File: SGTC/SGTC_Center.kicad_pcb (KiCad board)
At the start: 2 copper layers, 152.4 x 63.5 mm, 17 parts, among them J1 Left, J2 Right, U1 ADS8691IPWR, U2 TMUX131RMG, U3 SN74HCS72QDRQ1, U4 74AHC1G00, U5 AD8421

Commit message: added schematic to new SGTC
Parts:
- moved U4 3.67 mm to (143.6, 109.8)
- moved J1 3.67 mm to (120.1, 98.2)
- moved R2 3.67 mm to (117.9, 100.7)
- moved C4 3.67 mm to (125.9, 106.9)
- moved C5 3.67 mm to (122.7, 100.7)
- moved C6 3.67 mm to (117.9, 108.2)
- moved J2 3.67 mm to (140.4, 111.0)
- moved U1 3.67 mm to (120.4, 104.5)
- moved U5 3.67 mm to (130.1, 105.3)
- moved U2 3.67 mm to (133.4, 102.1)
- moved C1 3.67 mm to (127.2, 102.8)
- moved C2 3.67 mm to (125.2, 102.8)
- moved C3 3.67 mm to (125.9, 105.3)
- moved C7 3.67 mm to (132.6, 107.0)
- moved C8 3.67 mm to (134.6, 107.0)
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
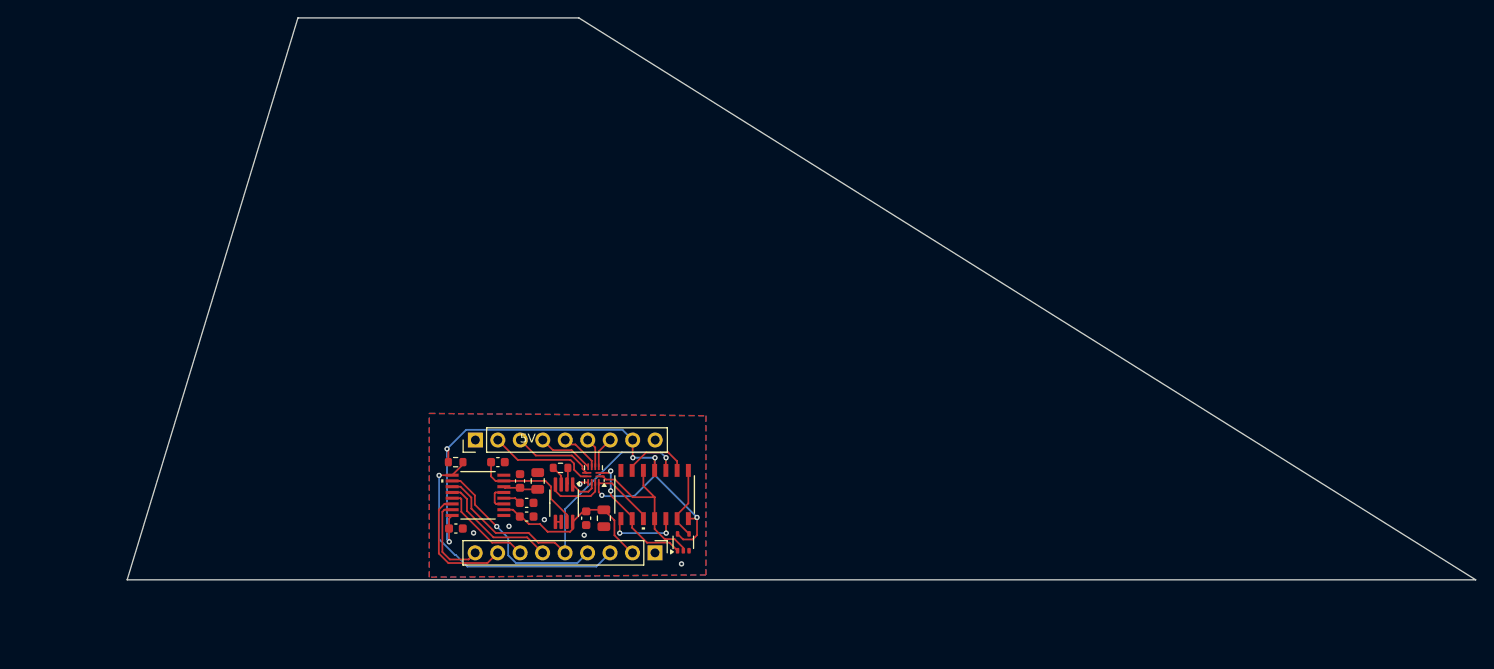
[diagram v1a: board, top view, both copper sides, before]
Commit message: fin center draft
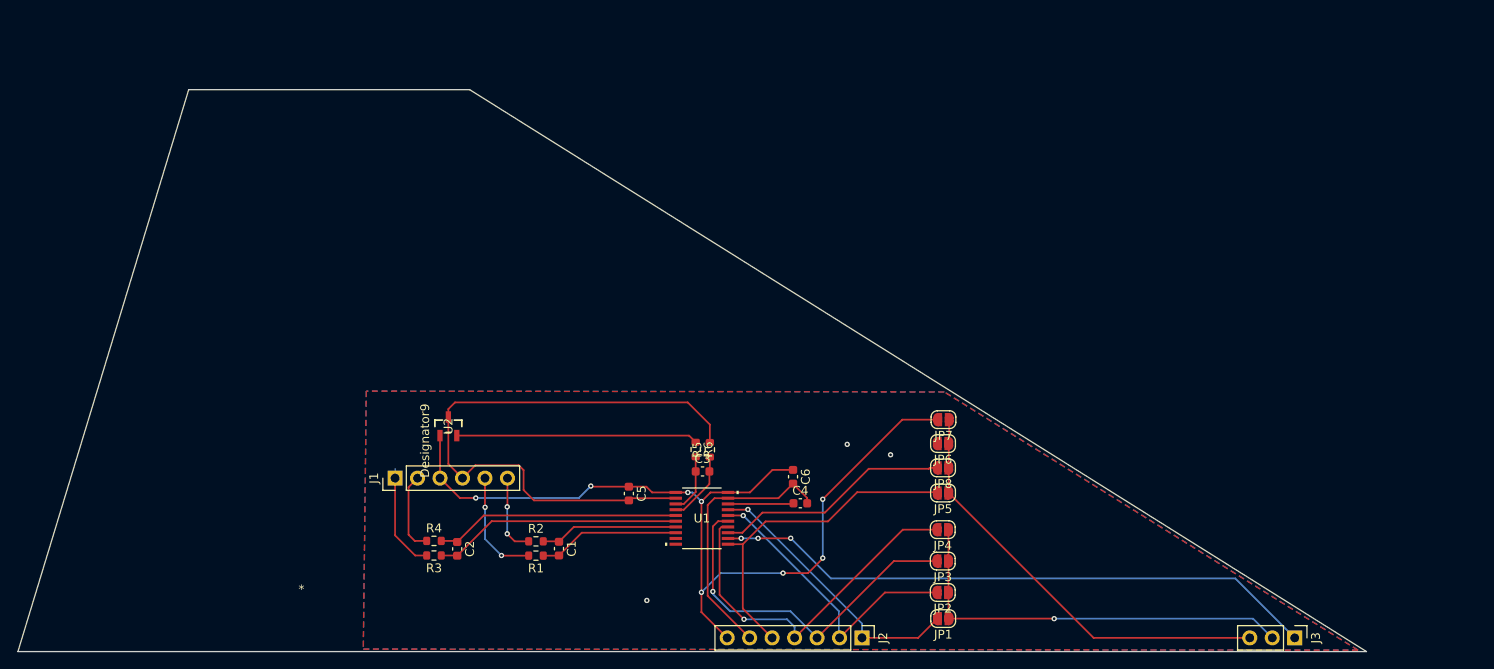
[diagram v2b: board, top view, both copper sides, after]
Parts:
- removed C7: 0.1 uF, Capacitor_SMD:C_0603_1608Metric
- removed C8: 10 uF, Capacitor_SMD:C_0805_2012Metric
- removed U3: SN74HCS72QDRQ1, strain-gauge:SOIC_QDRQ1_TEX
- removed U4: 74AHC1G00, Package_TO_SOT_SMD:SOT-353_SC-70-5
- removed U5: AD8421, Package_SO:MSOP-8_3x3mm_P0.65mm
- added J3: Conn_01x03_Pin, Connector_PinHeader_2.54mm:PinHeader_1x03_P2.54mm_Vertical, F.Cu at (212.7, 120.6)
- added JP1: SolderJumper_2_Open, Jumper:SolderJumper-2_P1.3mm_Open_RoundedPad1.0x1.5mm, F.Cu at (173.0, 118.4)
- added JP2: SolderJumper_2_Open, Jumper:SolderJumper-2_P1.3mm_Open_RoundedPad1.0x1.5mm, F.Cu at (172.9, 115.4)
- added JP3: SolderJumper_2_Open, Jumper:SolderJumper-2_P1.3mm_Open_RoundedPad1.0x1.5mm, F.Cu at (172.9, 111.9)
- added JP4: SolderJumper_2_Open, Jumper:SolderJumper-2_P1.3mm_Open_RoundedPad1.0x1.5mm, F.Cu at (172.9, 108.3)
- added JP5: SolderJumper_2_Open, Jumper:SolderJumper-2_P1.3mm_Open_RoundedPad1.0x1.5mm, F.Cu at (172.9, 104.2)
- added JP6: SolderJumper_2_Open, Jumper:SolderJumper-2_P1.3mm_Open_RoundedPad1.0x1.5mm, F.Cu at (172.9, 98.6)
- added JP7: SolderJumper_2_Open, Jumper:SolderJumper-2_P1.3mm_Open_RoundedPad1.0x1.5mm, F.Cu at (173.0, 95.9)
- added JP8: SolderJumper_2_Open, Jumper:SolderJumper-2_P1.3mm_Open_RoundedPad1.0x1.5mm, F.Cu at (172.9, 101.3)
- added R3: 10 k, Resistor_SMD:R_0603_1608Metric, F.Cu at (115.4, 111.2)
- added R4: 10 k, Resistor_SMD:R_0603_1608Metric, F.Cu at (115.4, 109.6)
- added R5: 10 k, Resistor_SMD:R_0603_1608Metric, F.Cu at (146.6, 99.3)
- added R6: 10 k, Resistor_SMD:R_0603_1608Metric, F.Cu at (145.0, 99.3)
- C1: value 10 uF -> 10 nF; footprint Capacitor_SMD:C_0805_2012Metric -> Capacitor_SMD:C_0603_1608Metric
- C2: value 1 uF -> 10 nF
- C3: value 4.7 uF -> 10 nF
- C4: value 1 uF -> 220 nF
- J1: value Left -> Conn_01x06_Pin; footprint Connector_PinHeader_2.54mm:PinHeader_1x09_P2.54mm_Vertical -> Connector_PinHeader_2.54mm:PinHeader_1x06_P2.54mm_Vertical
- J2: value Right -> Conn_01x07_Pin; footprint Connector_PinHeader_2.54mm:PinHeader_1x09_P2.54mm_Vertical -> Connector_PinHeader_2.54mm:PinHeader_1x07_P2.54mm_Vertical
- R1: value 100 -> 10 k
- R2: value 100k -> 10 k
- U1: value ADS8691IPWR -> ADS131M03QPWRQ1; footprint strain-gauge:PW16_TEX -> FinLib:ADS131M03
- U2: value TMUX131RMG -> TMP235A4DBZR; footprint Package_DFN_QFN:Texas_RMG0012A_WQFN-12_1.8x1.8mm_P0.4mm -> FinLib:TMP235A4DBZR
- moved C6 38.5 mm to (156.0, 102.3), turned to -90 degrees
- moved C4 31.0 mm to (156.8, 105.3)
- moved U1 25.4 mm to (145.7, 107.0), turned to 0 degrees
- moved J2 25.3 mm to (163.8, 120.6)
- moved C3 20.2 mm to (145.8, 101.8)
- moved U2 17.3 mm to (117.0, 96.7), turned to 90 degrees
- moved C5 15.2 mm to (137.4, 104.2), turned to -90 degrees
- moved R2 12.7 mm to (127.0, 109.7), turned to 0 degrees
- moved C2 10.5 mm to (118.0, 110.5)
- moved R1 10.3 mm to (127.0, 111.3)
- moved J1 10.0 mm to (111.0, 102.5)
- moved C1 8.02 mm to (129.6, 110.5)
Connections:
- net /ADC/~{CS} renamed ~{SYNC}/~{RST}
- C1 pad 1: GND -> Net-(U1-AIN2P)
- C1 pad 2: Net-(U1-REFCAP) -> Net-(U1-AIN2N)
- C2 pad 1: GND -> Net-(U1-AIN1N)
- C2 pad 2: Net-(U1-REFCAP) -> Net-(U1-AIN1P)
- C3 pad 1: Net-(U1-REFIO) -> Net-(U1-AIN0P)
- C3 pad 2: GND -> Net-(U1-AIN0N)
- C4 pad 1: +5V -> Net-(U1-CAP)
- C4 pad 2: GND -> TMP_IN_N
- C5 pad 1: /ADC/A_IN -> +3.3V
- C5 pad 2: GND -> TMP_IN_N
- C6 pad 1: GND -> +3.3V
- C6 pad 2: +3.3V -> TMP_IN_N
- J1 pad 1: GND -> GAUGE1_IN_N
- J1 pad 2: /Multiplexer/A_IN_N1 -> GAUGE1_IN_P
- J1 pad 3: /Multiplexer/A_IN_P1 -> +3.3V
- J1 pad 4: /Multiplexer/A_IN_N3 -> TMP_IN_N
- J1 pad 5: /Multiplexer/A_IN_P3 -> GAUGE2_IN_N
- J1 pad 6: /Multiplexer/A_IN_N2 -> GAUGE2_IN_P
- J2 pad 1: GND -> ADCCLK
- J2 pad 2: +5V -> DIN
- J2 pad 3: /ADC/~{RST} -> DOUT
- J2 pad 4: /ADC/SDI -> SPICLK
- J2 pad 6: /ADC/SCLK -> TMP_IN_N
- J2 pad 7: /ADC/SDO-0 -> +3.3V
- R1 pad 1: Net-(R1-Pad1) -> Net-(U1-AIN2N)
- R1 pad 2: Net-(R1-Pad2) -> GAUGE2_IN_N
- R2 pad 1: /ADC/~{RST} -> GAUGE2_IN_P
- R2 pad 2: +3.3V -> Net-(U1-AIN2P)
- U1 pad 1: GND -> +3.3V
- U1 pad 10: /ADC/SDI -> unconnected-(U1-NC-Pad10)
- U1 pad 12: /ADC/SCLK -> ~{CS}
- U1 pad 13: /ADC/SDO-0 -> ~{DRDY}
- U1 pad 14: /ADC/SDO-1 -> SPICLK
- U1 pad 15: /ADC/RVS -> DOUT
- U1 pad 16: +3.3V -> DIN
- U1 pad 2: +5V -> TMP_IN_N
- U1 pad 3: GND -> Net-(U1-AIN0P)
- U1 pad 4: Net-(U1-REFIO) -> Net-(U1-AIN0N)
- U1 pad 5: GND -> Net-(U1-AIN1N)
- U1 pad 6: Net-(U1-REFCAP) -> Net-(U1-AIN1P)
- U1 pad 7: /ADC/A_IN -> Net-(U1-AIN2P)
- U1 pad 8: GND -> Net-(U1-AIN2N)
- U1 pad 9: /ADC/~{RST} -> unconnected-(U1-NC-Pad9)
- U2 pad 1: /Counter/SEL0 -> +3.3V
- U2 pad 2: /Counter/SEL1 -> TMP_IN_P
- U2 pad 3: /Multiplexer/A_IN_P2 -> TMP_IN_N
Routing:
- net TMP_IN_N: track 0.00 -> 99.7 mm, vias 0 -> 3
- net ~{CS}: track 0.00 -> 68.7 mm, vias 0 -> 3
- net Net-(J3-Pin_3): track 0.00 -> 49.1 mm
- net Net-(J3-Pin_2): track 0.00 -> 47.5 mm, vias 0 -> 1
- net SPICLK: track 0.00 -> 40.9 mm, vias 0 -> 1
- net DOUT: track 0.00 -> 40.6 mm, vias 0 -> 1
- net DIN: track 0.00 -> 33.2 mm, vias 0 -> 1
- net /ADC/~{RST}: track 31.9 -> 0.00 mm, vias 1 -> 0
- net ADCCLK: track 0.00 -> 31.5 mm, vias 0 -> 1
- net +3.3V: track 73.6 -> 103.8 mm, vias 6 -> 8
- net Net-(U1-AIN1P): track 0.00 -> 28.1 mm
- net Net-(U1-AIN1N): track 0.00 -> 27.8 mm
- net TMP_IN_P: track 0.00 -> 27.3 mm
- net ~{DRDY}: track 0.00 -> 26.7 mm
- net /ADC/SDI: track 21.4 -> 0.00 mm, vias 1 -> 0
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- added copper zone on B.Cu, net TMP_IN_N
- added copper zone on F.Cu, net TMP_IN_N
- removed copper zone on B.Cu, net GND
- removed copper zone on F.Cu, net GND
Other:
- outline, holes or cut-outs redrawn
- board text removed: "5V"

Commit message: silkscreen things mostly
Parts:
- moved C6 3.51 mm to (152.5, 102.6)
- moved JP4 1.67 mm to (173.0, 110.0)
- moved R3 1.65 mm to (115.5, 109.6), turned to 0 degrees
- moved R5 1.60 mm to (145.0, 99.2), turned to -90 degrees
- moved R4 1.60 mm to (115.5, 111.2), turned to 180 degrees
- moved R6 1.60 mm to (146.6, 99.2), turned to 90 degrees
- moved JP3 1.37 mm to (173.0, 113.2)
- moved JP1 1.37 mm to (173.0, 119.8)
- moved JP2 1.07 mm to (173.0, 116.5)
- moved JP5 0.61 mm to (173.0, 104.8)
- moved JP8 0.61 mm to (173.0, 102.0)
- moved JP6 0.60 mm to (173.0, 99.2)
- moved JP7 0.55 mm to (173.0, 96.5)
- moved C4 0.15 mm to (156.8, 105.2)
- moved C2 0.11 mm to (118.0, 110.4)
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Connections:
- C4 pad 2: TMP_IN_N -> GND
- C5 pad 2: TMP_IN_N -> GND
- C6 pad 2: TMP_IN_N -> GND
- J1 pad 4: TMP_IN_N -> GND
- J2 pad 6: TMP_IN_N -> GND
- JP1 pad 1: Net-(J3-Pin_2) -> Net-(J3-Pin_3)
- JP2 pad 1: Net-(J3-Pin_2) -> Net-(J3-Pin_3)
- JP3 pad 1: Net-(J3-Pin_2) -> Net-(J3-Pin_3)
- JP4 pad 1: Net-(J3-Pin_2) -> Net-(J3-Pin_3)
- JP5 pad 1: Net-(J3-Pin_3) -> Net-(J3-Pin_2)
- JP6 pad 1: Net-(J3-Pin_3) -> Net-(J3-Pin_2)
- JP6 pad 2: TMP_IN_N -> GND
- JP7 pad 1: Net-(J3-Pin_3) -> Net-(J3-Pin_2)
- JP8 pad 1: Net-(J3-Pin_3) -> Net-(J3-Pin_2)
- R3 pad 1: Net-(U1-AIN1P) -> GAUGE1_IN_P
- R3 pad 2: GAUGE1_IN_N -> Net-(U1-AIN1N)
- R4 pad 1: GAUGE1_IN_P -> Net-(U1-AIN1P)
- R4 pad 2: Net-(U1-AIN1N) -> GAUGE1_IN_N
- R5 pad 1: Net-(U1-AIN0N) -> TMP_IN_P
- R5 pad 2: TMP_IN_N -> Net-(U1-AIN0P)
- R6 pad 1: TMP_IN_P -> Net-(U1-AIN0N)
- R6 pad 2: Net-(U1-AIN0P) -> GND
- U1 pad 19: TMP_IN_N -> GND
- U1 pad 2: TMP_IN_N -> GND
- U2 pad 3: TMP_IN_N -> GND
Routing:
- net TMP_IN_N: track 99.7 -> 0.00 mm, vias 3 -> 0
- net +3.3V: track 103.8 -> 83.6 mm, vias 8 -> 4
- net Net-(J3-Pin_3): track 49.1 -> 44.0 mm
- net Net-(J3-Pin_2): track 47.5 -> 51.3 mm, vias 1 -> 0
- net GND: track 0.00 -> 1.23 mm, vias 0 -> 11
- net GAUGE1_IN_N: track 12.1 -> 11.0 mm
- net SPICLK: track 40.9 -> 40.2 mm
- net ADCCLK: track 31.5 -> 31.0 mm
- net DOUT: track 40.6 -> 40.1 mm
- net Net-(U1-AIN0N): track 8.08 -> 8.59 mm
- added copper zone on B.Cu, net GND
- added copper zone on F.Cu, net GND
- removed copper zone on B.Cu, net TMP_IN_N
- removed copper zone on F.Cu, net TMP_IN_N
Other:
- board text added: "3.3V"
- board text added: "CLK"
- board text added: "DIN"
- board text added: "DOUT"
- board text added: "GND"
- board text added: "SCK"
- board text added: "~{CS}"
- board text added: "~{DRDY}"
- board text added: "~{RST}"

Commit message: final version
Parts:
- added J4: Conn_01x01_Pin, Connector_PinHeader_2.54mm:PinHeader_1x01_P2.54mm_Vertical, F.Cu at (156.2, 120.7)
- added J5: Conn_01x01_Pin, Connector_PinHeader_2.54mm:PinHeader_1x01_P2.54mm_Vertical, F.Cu at (148.6, 120.7)
- added J6: Conn_01x01_Pin, Connector_PinHeader_2.54mm:PinHeader_1x01_P2.54mm_Vertical, F.Cu at (141.0, 120.7)
- added J7: Conn_01x01_Pin, Connector_PinHeader_2.54mm:PinHeader_1x01_P2.54mm_Vertical, F.Cu at (133.3, 120.7)
- added J8: Conn_01x01_Pin, Connector_PinHeader_2.54mm:PinHeader_1x01_P2.54mm_Vertical, F.Cu at (125.7, 120.7)
- added J9: Conn_01x01_Pin, Connector_PinHeader_2.54mm:PinHeader_1x01_P2.54mm_Vertical, F.Cu at (118.1, 120.7)
- J2: value Conn_01x07_Pin -> Conn_01x01_Pin; footprint Connector_PinHeader_2.54mm:PinHeader_1x07_P2.54mm_Vertical -> Connector_PinHeader_2.54mm:PinHeader_1x01_P2.54mm_Vertical
- moved J2 0.05 mm to (163.8, 120.7), turned to 0 degrees
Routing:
- net +3.3V: track 83.6 -> 105.6 mm
- net ~{SYNC}/~{RST}: track 37.8 -> 51.3 mm, vias 0 -> 1
- net SPICLK: track 40.2 -> 52.3 mm, vias 1 -> 3
- net DIN: track 32.8 -> 35.9 mm
- net DOUT: track 40.1 -> 42.1 mm, vias 1 -> 0
- net GND: vias 11 -> 13

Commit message: fixed core dimensions and pin locations
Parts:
- removed J1: Conn_01x06_Pin, Connector_PinHeader_2.54mm:PinHeader_1x06_P2.54mm_Vertical
- added J10: Conn_01x04_Pin, Connector_PinHeader_2.54mm:PinHeader_1x04_P2.54mm_Vertical, F.Cu at (70.9, 138.5)
- added J11: Conn_01x04_Pin, Connector_PinHeader_2.54mm:PinHeader_1x04_P2.54mm_Vertical, F.Cu at (153.7, 138.7)
- moved J2 36.0 mm to (132.6, 138.6)
- moved C3 36.0 mm to (114.6, 119.7)
- moved C5 36.0 mm to (106.2, 122.2)
- moved J4 36.0 mm to (125.0, 138.6)
- moved C1 36.0 mm to (98.3, 128.3)
- moved C2 36.0 mm to (86.8, 128.3)
- moved C4 36.0 mm to (125.6, 123.1)
- moved C6 36.0 mm to (121.3, 120.5)
- moved J3 36.0 mm to (181.5, 138.4)
- moved J5 36.0 mm to (117.4, 138.6)
- moved J6 36.0 mm to (109.8, 138.6)
- moved J7 36.0 mm to (102.2, 138.6)
- moved J8 36.0 mm to (94.5, 138.6)
- moved J9 36.0 mm to (86.9, 138.6)
- moved JP1 36.0 mm to (141.8, 137.7)
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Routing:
- net +3.3V: track 105.6 -> 183.6 mm, vias 4 -> 7
- net GAUGE2_IN_P: track 9.08 -> 84.1 mm, vias 2 -> 5
- net GAUGE2_IN_N: track 12.6 -> 87.2 mm, vias 2 -> 3
- net GAUGE1_IN_N: track 11.0 -> 1.30 mm
- net GAUGE1_IN_P: track 9.15 -> 1.35 mm
- net Net-(J3-Pin_3): track 44.0 -> 45.3 mm
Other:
- board size 152.4 x 63.5 mm -> 264.1 x 101.6 mm

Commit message: update fins with bridge completion resistors
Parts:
- added R2: 1 k, Resistor_SMD:R_0603_1608Metric, F.Cu at (83.2, 133.2)
- added R8: 1 k, Resistor_SMD:R_0603_1608Metric, F.Cu at (156.5, 134.2)
- added R9: 1 k, Resistor_SMD:R_0603_1608Metric, F.Cu at (150.5, 136.0)
- C2: value 10 nF -> 5 nF
- C4: renamed from C1; value 10 nF -> 5 nF
- R3: renamed from R6; value 10 k -> 1 k
- R4: renamed from R3; value 10 k -> 5 k
- R5: renamed from R4; value 10 k -> 5 k
- R6: renamed from R2; value 10 k -> 5 k
- R7: renamed from R1; value 10 k -> 5 k
- moved R3 34.3 mm to (82.0, 124.8), turned to -90 degrees
- moved J10 1.90 mm to (153.7, 136.8)
- renumbered C3 to C1, C5 to C3, C6 to C5, C4 to C6, J2 to J1, J11 to J10, J4 to J2, J5 to J3, J6 to J4, J7 to J5, J8 to J6, J9 to J7, J3 to J8, J10 to J9, JP5 to JP1, JP6 to JP2, JP7 to JP3, JP8 to JP4, JP1 to JP5, JP2 to JP6, JP3 to JP7, JP4 to JP8, R5 to R1
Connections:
- C1 pad 2: Net-(U1-AIN0N) -> GND
- J9 pad 1: GAUGE1_IN_P -> GAUGE1_IN_N
- J9 pad 2: GAUGE1_IN_N -> GAUGE1_IN_P
- R3 pad 1: Net-(U1-AIN0N) -> GND
- R3 pad 2: GND -> GAUGE1_IN_N
- R4 pad 1: GAUGE1_IN_P -> GAUGE1_IN_N
- R5 pad 2: GAUGE1_IN_N -> GAUGE1_IN_P
- U1 pad 4: Net-(U1-AIN0N) -> GND
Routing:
- net +3.3V: track 183.6 -> 149.3 mm
- net GAUGE1_IN_P: track 1.35 -> 15.7 mm
- net Net-(J8-Pin_3): track 45.3 -> 34.3 mm
- net Net-(U1-AIN0N): track 8.59 -> 0.00 mm
- net Net-(J8-Pin_2): track 51.3 -> 43.0 mm
- net GND: track 1.23 -> 8.24 mm, vias 13 -> 17
- net GAUGE2_IN_N: track 87.2 -> 91.3 mm
- net GAUGE1_IN_N: track 1.30 -> 3.34 mm
- net GAUGE2_IN_P: track 84.1 -> 86.0 mm, vias 5 -> 4
- added copper zone on F.Cu, net Net-(J8-Pin_2)
- added copper zone on F.Cu, net Net-(J8-Pin_3)
